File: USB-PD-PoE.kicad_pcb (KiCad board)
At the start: 4 copper layers, 39.6 x 87.4 mm, 126 parts, among them J1 8P8C_Shielded, J2 8P8C_Shielded, J3 TagConnect_TC2030_SWD, J4 USB_C_Receptacle_USB2.0, Q1 FDC2512, Q2 2N7002, Q3 2N7002, Q4 2N7002, Q5 APM4953KC, T1 HR051142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

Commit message: Improve VBUS current carrying capability
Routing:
- net VBUS: track 146.8 -> 153.8 mm
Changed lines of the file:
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@@
     (thickness 1.6)
     (drawings 40)
-    (tracks 2094)
+    (tracks 2096)
     (zones 0)
     (modules 126)
@@
   )
   (setup
-    (last_trace_width 0.127)
+    (last_trace_width 1)
     (user_trace_width 0.09)
     (user_trace_width 0.127)
@@
   (segment (start 114.1 67.5) (end 113.35 67.5) (width 1) (layer F.Cu) (net 94))
   (segment (start 114.1 68.85) (end 113.35 68.85) (width 1) (layer F.Cu) (net 94))
+  (segment (start 114.1 68.85) (end 112.8 70.15) (width 1) (layer F.Cu) (net 94))
+  (segment (start 112.8 70.15) (end 107.65 70.15) (width 1) (layer F.Cu) (net 94))
   (via (at 125.025 76.475) (size 0.45) (drill 0.2) (layers F.Cu B.Cu) (net 95))
   (segment (start 125.125 76.575) (end 125.025 76.475) (width 0.127) (layer F.Cu) (net 95))

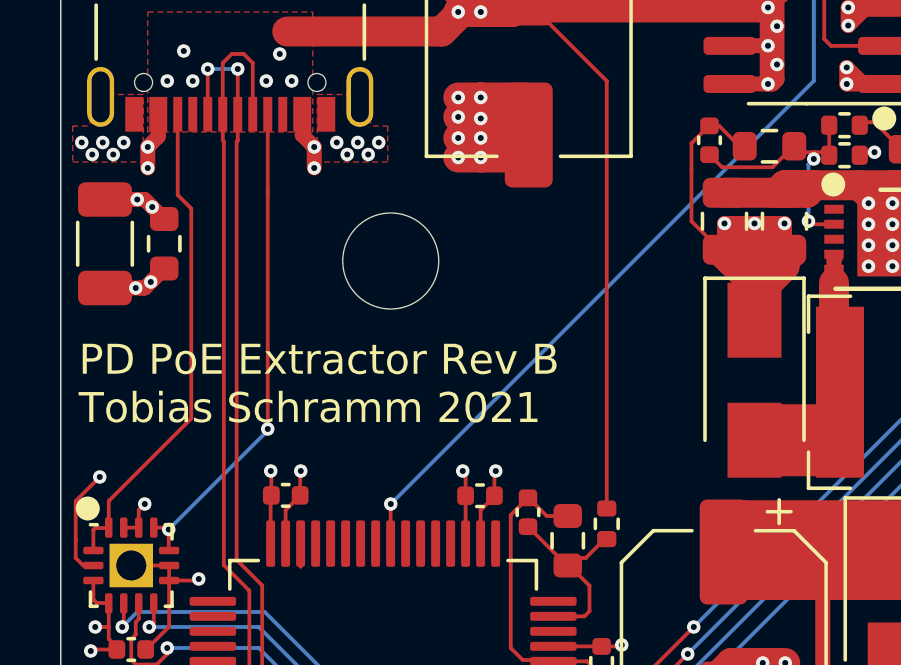
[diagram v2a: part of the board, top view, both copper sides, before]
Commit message: Protect screw holes from layer shorts
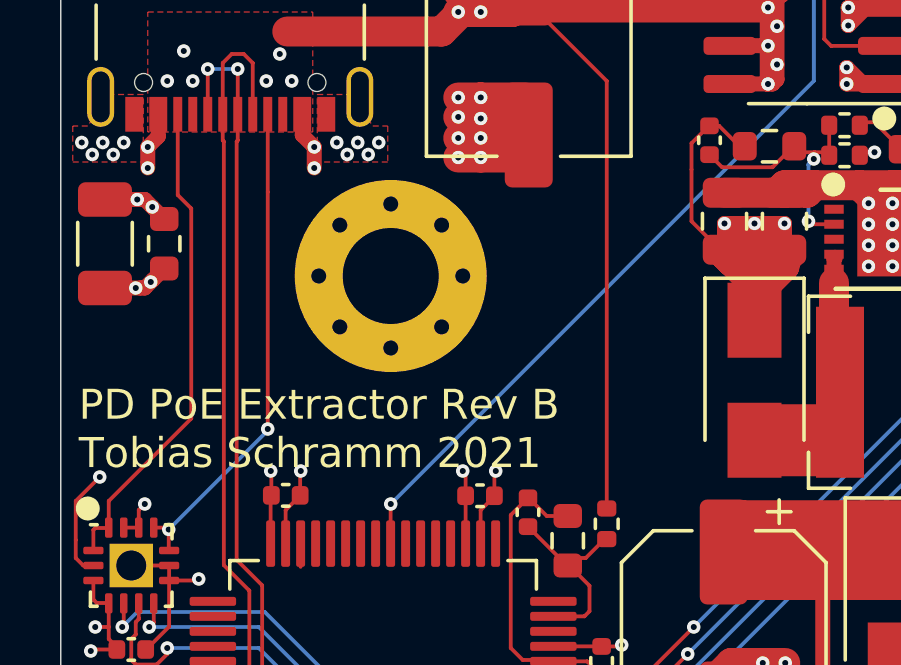
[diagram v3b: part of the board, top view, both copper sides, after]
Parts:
- H2: footprint MountingHole:MountingHole_3.2mm_M3 -> MountingHole:MountingHole_3.2mm_M3_Pad_Via
- moved H2 0.50 mm to (111.1, 78.3)
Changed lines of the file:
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@@
     (add_net VBUS)
   )
+  (module MountingHole:MountingHole_3.2mm_M3 (layer F.Cu)
+    (at 121.25 109.775)
+    (descr "Mounting Hole 3.2mm, no annular, M3")
+    (tags "mounting hole 3.2mm no annular m3")
+    (clearance 1)
+    (attr virtual)
+    (fp_text reference H1 (at 0 -4.2) (layer F.SilkS) hide
+      (effects (font (size 1 1) (thickness 0.15)))
+    )
+    (fp_text value MountingHole (at 0 4.2) (layer F.Fab)
+      (effects (font (size 1 1) (thickness 0.15)))
+    )
+    (fp_text user %R (at 0.3 0) (layer F.Fab)
+      (effects (font (size 1 1) (thickness 0.15)))
+    )
+    (fp_circle (center 0 0) (end 3.2 0) (layer Cmts.User) (width 0.15))
+    (fp_circle (center 0 0) (end 3.45 0) (layer F.CrtYd) (width 0.05))
+    (pad 1 np_thru_hole circle (at 0 0) (size 3.2 3.2) (drill 3.2) (layers *.Cu *.Mask))
+  )
+  (module MountingHole:MountingHole_3.2mm_M3_Pad_Via (layer F.Cu)
+    (at 111.1 78.3)
+    (descr "Mounting Hole 3.2mm, M3")
+    (tags "mounting hole 3.2mm m3")
+    (attr virtual)
+    (fp_text reference H2 (at 0 -4.2) (layer F.SilkS) hide
+      (effects (font (size 1 1) (thickness 0.15)))
+    )
+    (fp_text value MountingHole (at 0 4.2) (layer F.Fab)
+      (effects (font (size 1 1) (thickness 0.15)))
+    )
+    (fp_text user %R (at 0.3 0) (layer F.Fab)
+      (effects (font (size 1 1) (thickness 0.15)))
+    )
+    (fp_circle (center 0 0) (end 3.2 0) (layer Cmts.User) (width 0.15))
+    (fp_circle (center 0 0) (end 3.45 0) (layer F.CrtYd) (width 0.05))
+    (pad 1 thru_hole circle (at 1.697056 -1.697056) (size 0.8 0.8) (drill 0.5) (layers *.Cu *.Mask))
+    (pad 1 thru_hole circle (at 0 -2.4) (size 0.8 0.8) (drill 0.5) (layers *.Cu *.Mask))
+    (pad 1 thru_hole circle (at -1.697056 -1.697056) (size 0.8 0.8) (drill 0.5) (layers *.Cu *.Mask))
+    (pad 1 thru_hole circle (at -2.4 0) (size 0.8 0.8) (drill 0.5) (layers *.Cu *.Mask))
+    (pad 1 thru_hole circle (at -1.697056 1.697056) (size 0.8 0.8) (drill 0.5) (layers *.Cu *.Mask))
+    (pad 1 thru_hole circle (at 0 2.4) (size 0.8 0.8) (drill 0.5) (layers *.Cu *.Mask))
+    (pad 1 thru_hole circle (at 1.697056 1.697056) (size 0.8 0.8) (drill 0.5) (layers *.Cu *.Mask))
+    (pad 1 thru_hole circle (at 2.4 0) (size 0.8 0.8) (drill 0.5) (layers *.Cu *.Mask))
+    (pad 1 thru_hole circle (at 0 0) (size 6.4 6.4) (drill 3.2) (layers *.Cu *.Mask))
+  )
   (module Package_DFN_QFN:WQFN-14-1EP_2.5x2.5mm_P0.5mm_EP1.45x1.45mm (layer F.Cu)
     (at 102.449999 87.95)
@@
     (pad "" np_thru_hole circle (at 0 0) (size 1.152 1.152) (drill 1.152) (layers *.Cu *.Mask))
   )
-  (module MountingHole:MountingHole_3.2mm_M3 (layer F.Cu)
-    (at 111.1 77.8)
-    (descr "Mounting Hole 3.2mm, no annular, M3")
-    (tags "mounting hole 3.2mm no annular m3")
-    (attr virtual)
-    (fp_text reference H2 (at 0 -4.2) (layer F.SilkS) hide
-      (effects (font (size 1 1) (thickness 0.15)))
-    )
-    (fp_text value MountingHole (at 0 4.2) (layer F.Fab)
-      (effects (font (size 1 1) (thickness 0.15)))
-    )
-    (fp_circle (center 0 0) (end 3.45 0) (layer F.CrtYd) (width 0.05))
-    (fp_circle (center 0 0) (end 3.2 0) (layer Cmts.User) (width 0.15))
-    (fp_text user %R (at 0.3 0) (layer F.Fab)
-      (effects (font (size 1 1) (thickness 0.15)))
-    )
-    (pad 1 np_thru_hole circle (at 0 0) (size 3.2 3.2) (drill 3.2) (layers *.Cu *.Mask))
-  )
   (module Package_SO:SO-8_3.9x4.9mm_P1.27mm (layer F.Cu)
     (at 124.975 69.995 180)
@@
     )
   )
-  (module MountingHole:MountingHole_3.2mm_M3 (layer F.Cu)
-    (at 121.25 109.775)
-    (descr "Mounting Hole 3.2mm, no annular, M3")
-    (tags "mounting hole 3.2mm no annular m3")
-    (attr virtual)
-    (fp_text reference H1 (at 0 -4.2) (layer F.SilkS) hide
-      (effects (font (size 1 1) (thickness 0.15)))
-    )
-    (fp_text value MountingHole (at 0 4.2) (layer F.Fab)
-      (effects (font (size 1 1) (thickness 0.15)))
-    )
-    (fp_circle (center 0 0) (end 3.45 0) (layer F.CrtYd) (width 0.05))
-    (fp_circle (center 0 0) (end 3.2 0) (layer Cmts.User) (width 0.15))
-    (fp_text user %R (at 0.3 0) (layer F.Fab)
-      (effects (font (size 1 1) (thickness 0.15)))
-    )
-    (pad 1 np_thru_hole circle (at 0 0) (size 3.2 3.2) (drill 3.2) (layers *.Cu *.Mask))
-  )
   (module Resistor_SMD:R_0402_1005Metric (layer F.Cu)
     (at 119.675 101.25 270)
@@
       (net 80 "Net-(C17-Pad2)"))
   )
-  (gr_text "PD PoE Extractor Rev B\nTobias Schramm 2021" (at 100.7 81.9) (layer F.SilkS)
+  (gr_text "PD PoE Extractor Rev B\nTobias Schramm 2021" (at 100.7 83.4) (layer F.SilkS)
     (effects (font (size 1 1) (thickness 0.15)) (justify left))
   )

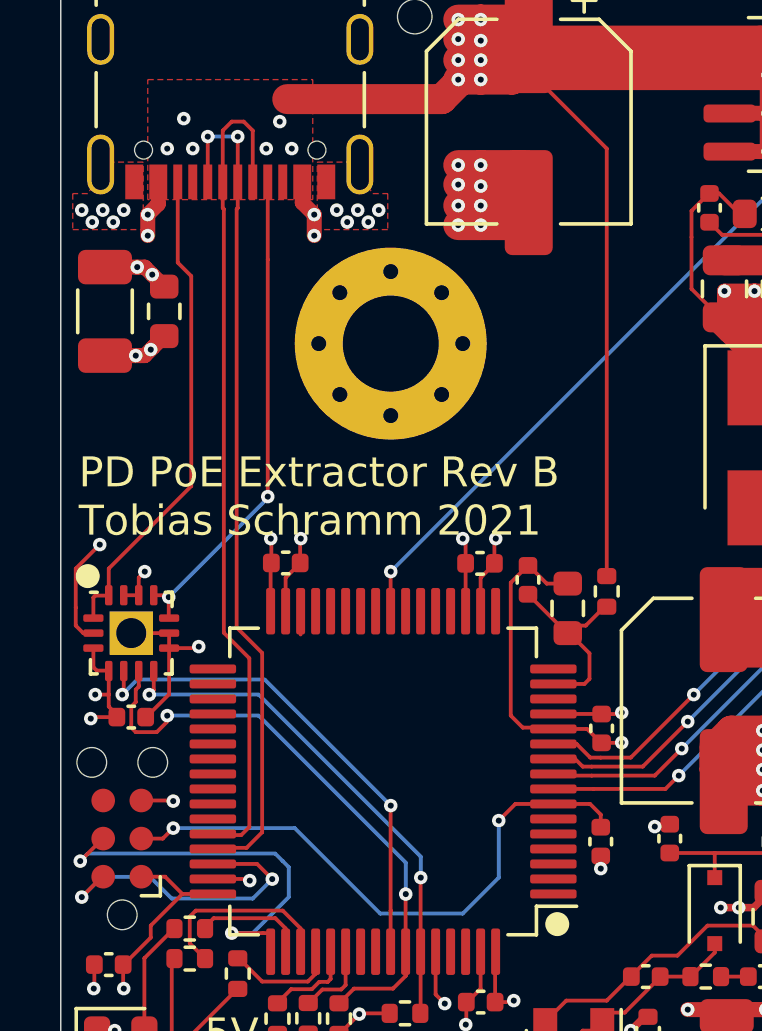
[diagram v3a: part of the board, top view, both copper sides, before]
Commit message: Add USB/CC protection diode
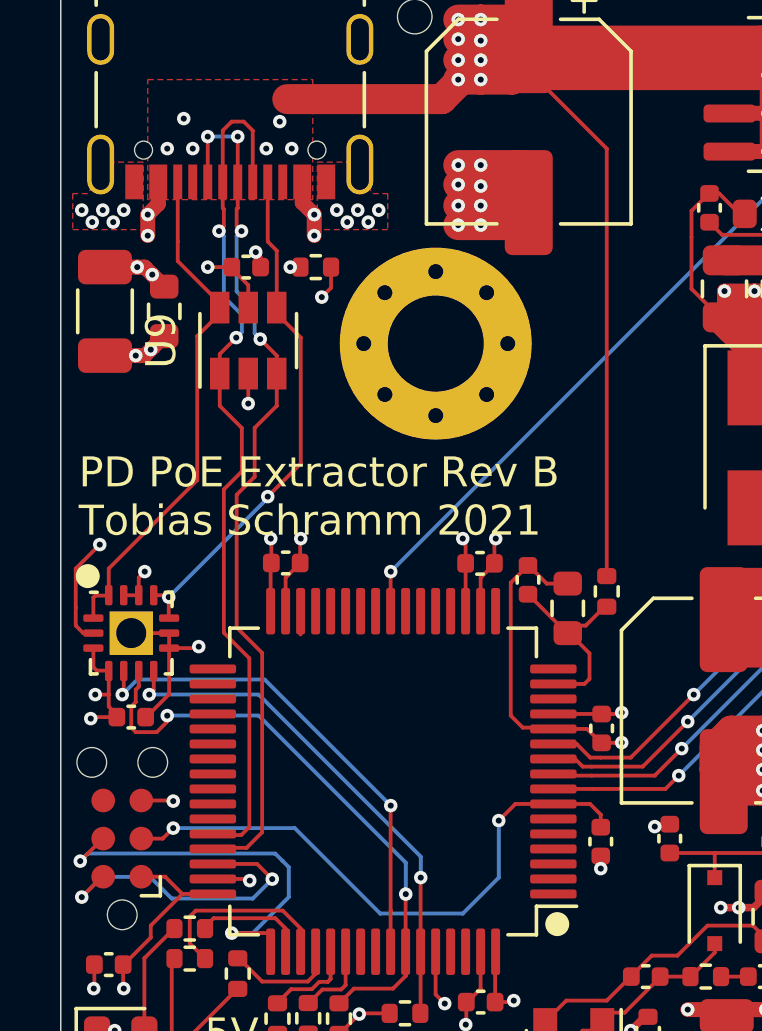
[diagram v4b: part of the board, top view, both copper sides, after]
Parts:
- added C40: 100nF, Capacitor_SMD:C_0402_1005Metric, F.Cu at (106.3, 75.8)
- added R49: 10kR, Resistor_SMD:R_0402_1005Metric, F.Cu at (108.6, 75.8)
- added U9: SRV05-4, Package_TO_SOT_SMD:SOT-23-6, F.Cu at (106.3, 78.2)
- moved H2 1.50 mm to (112.6, 78.3)
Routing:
- net +12V: track 134.4 -> 161.7 mm, vias 19 -> 20
- net Net-(C40-Pad1): track 0.00 -> 5.42 mm, vias 0 -> 2
- net GND: track 149.7 -> 151.2 mm, vias 78 -> 80
- net /D+: track 27.9 -> 29.2 mm, vias 2 -> 4
- net /D-: track 27.9 -> 29.1 mm, vias 0 -> 2
- net /CC1: track 16.4 -> 17.4 mm
- net /CC2: track 16.3 -> 17.1 mm
